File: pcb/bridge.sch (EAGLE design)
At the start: 31 parts, among them IC1 ARDUINO_PRO_MICRO, IC2 LM358D, X1 SZARKBUS, X2 RSENSE, X3 +12V

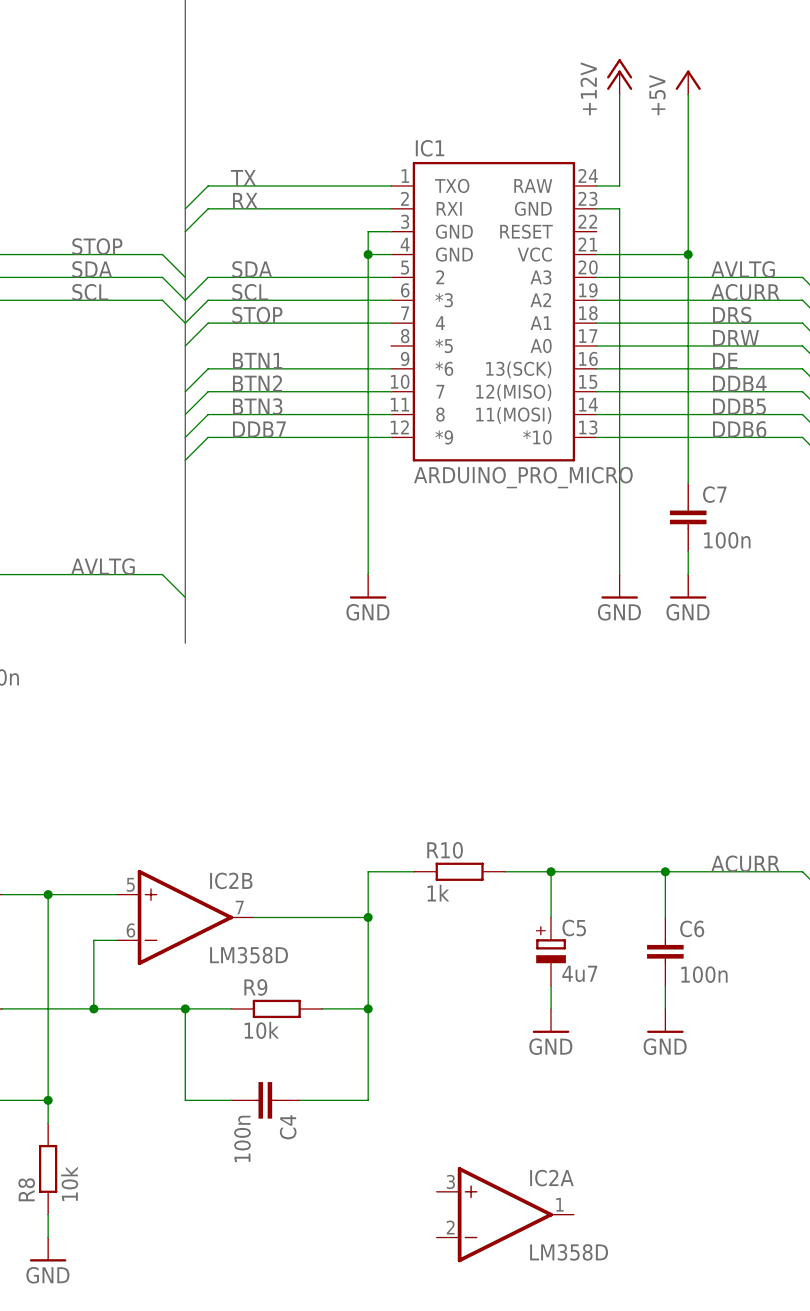
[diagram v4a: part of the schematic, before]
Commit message: bridge: Connect unused op-amp to the ground.
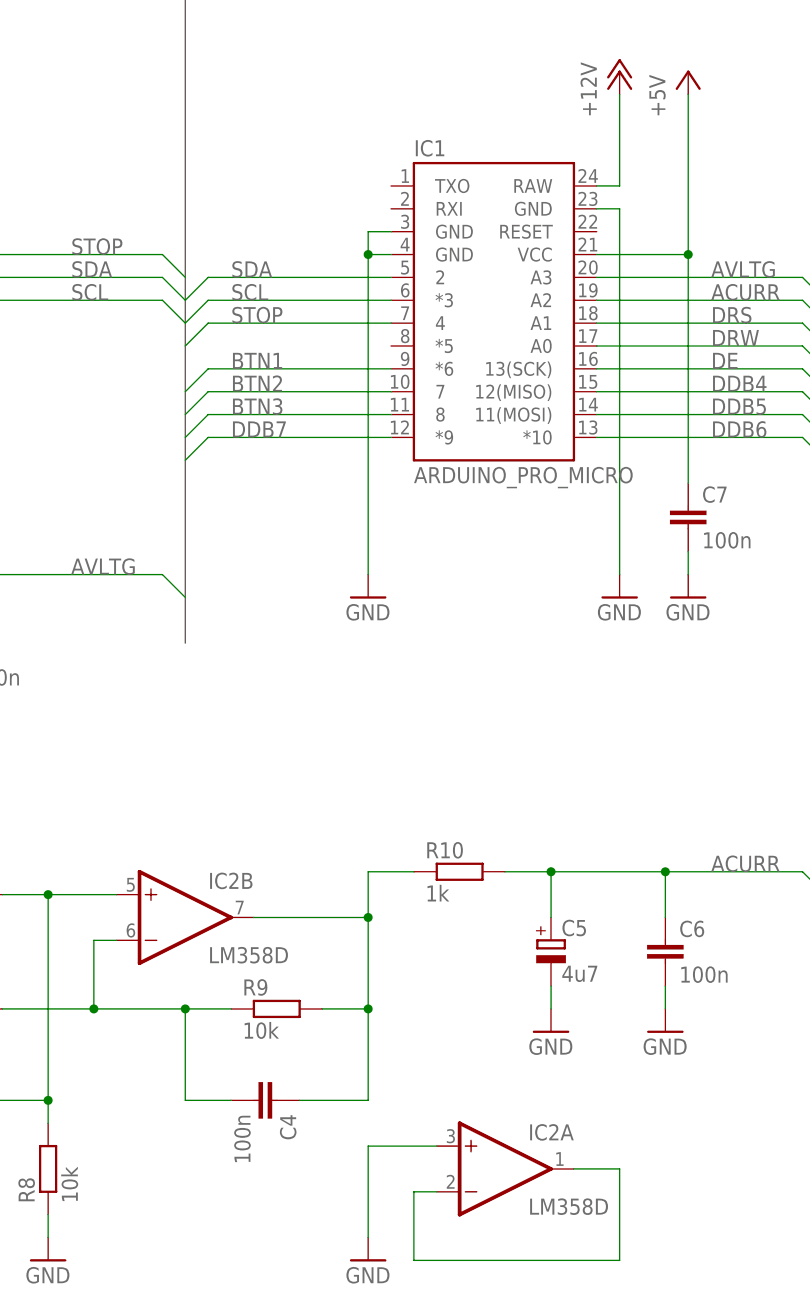
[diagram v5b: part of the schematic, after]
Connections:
- removed net RX: IC1.RXI
- removed net TX: IC1.TXO
- new net N$12: IC2A.-IN, IC2A.OUT
- net GND: now also IC2A.+IN
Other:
- moved on the sheet: IC2A
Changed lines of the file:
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@@
 <part name="C7" library="rcl" deviceset="C-EU" device="C1206" value="100n"/>
 <part name="GND15" library="supply1" deviceset="GND" device=""/>
+<part name="GND16" library="supply1" deviceset="GND" device=""/>
 </parts>
 <sheets>
@@
 <instance part="GND20" gate="1" x="215.9" y="35.56"/>
 <instance part="P+11" gate="1" x="215.9" y="66.04"/>
-<instance part="IC2" gate="A" x="139.7" y="20.32"/>
+<instance part="IC2" gate="A" x="139.7" y="25.4"/>
 <instance part="IC2" gate="B" x="104.14" y="53.34"/>
 <instance part="R6" gate="G$1" x="78.74" y="55.88"/>
@@
 <instance part="C7" gate="G$1" x="160.02" y="99.06"/>
 <instance part="GND15" gate="1" x="160.02" y="88.9"/>
+<instance part="GND16" gate="1" x="124.46" y="15.24"/>
 </instances>
 <busses>
@@
 <pinref part="GND15" gate="1" pin="GND"/>
 <wire x1="160.02" y1="91.44" x2="160.02" y2="93.98" width="0.1524" layer="91"/>
+</segment>
+<segment>
+<pinref part="IC2" gate="A" pin="+IN"/>
+<pinref part="GND16" gate="1" pin="GND"/>
+<wire x1="132.08" y1="27.94" x2="124.46" y2="27.94" width="0.1524" layer="91"/>
+<wire x1="124.46" y1="27.94" x2="124.46" y2="17.78" width="0.1524" layer="91"/>
 </segment>
 </net>
@@
 </segment>
 </net>
-<net name="RX" class="0">
-<segment>
-<wire x1="104.14" y1="129.54" x2="106.68" y2="132.08" width="0.1524" layer="91"/>
-<pinref part="IC1" gate="G$1" pin="RXI"/>
-<wire x1="106.68" y1="132.08" x2="127" y2="132.08" width="0.1524" layer="91"/>
-<label x="109.22" y="132.08" size="1.778" layer="95"/>
-</segment>
-</net>
 <net name="SDA" class="0">
 <segment>
@@
 </segment>
 </net>
-<net name="TX" class="0">
-<segment>
-<wire x1="104.14" y1="132.08" x2="106.68" y2="134.62" width="0.1524" layer="91"/>
-<pinref part="IC1" gate="G$1" pin="TXO"/>
-<wire x1="106.68" y1="134.62" x2="127" y2="134.62" width="0.1524" layer="91"/>
-<label x="109.22" y="134.62" size="1.778" layer="95"/>
-</segment>
-</net>
 <net name="BTN3" class="0">
 <segment>
@@
 </segment>
 </net>
+<net name="N$12" class="0">
+<segment>
+<pinref part="IC2" gate="A" pin="OUT"/>
+<wire x1="147.32" y1="25.4" x2="152.4" y2="25.4" width="0.1524" layer="91"/>
+<wire x1="152.4" y1="25.4" x2="152.4" y2="15.24" width="0.1524" layer="91"/>
+<wire x1="152.4" y1="15.24" x2="129.54" y2="15.24" width="0.1524" layer="91"/>
+<wire x1="129.54" y1="15.24" x2="129.54" y2="22.86" width="0.1524" layer="91"/>
+<pinref part="IC2" gate="A" pin="-IN"/>
+<wire x1="129.54" y1="22.86" x2="132.08" y2="22.86" width="0.1524" layer="91"/>
+</segment>
+</net>
 </nets>
 </sheet>
 </sheets>
+<errors>
+</errors>
 </schematic>
 </drawing>

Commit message: bridge: Update resistor values.
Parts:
- C1, C5: value 4u7 -> 22u
- R2: value 470 -> 1k
- R6, R7: value 8k2 -> 4k7
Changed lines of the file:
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@@
 <part name="P+11" library="supply1" deviceset="+12V" device=""/>
 <part name="IC2" library="linear" deviceset="LM358" device="D"/>
-<part name="R6" library="rcl" deviceset="R-EU_" device="M1206" value="8k2"/>
-<part name="R7" library="rcl" deviceset="R-EU_" device="M1206" value="8k2"/>
+<part name="R6" library="rcl" deviceset="R-EU_" device="M1206" value="4k7"/>
+<part name="R7" library="rcl" deviceset="R-EU_" device="M1206" value="4k7"/>
 <part name="R8" library="rcl" deviceset="R-EU_" device="M1206" value="10k"/>
 <part name="R9" library="rcl" deviceset="R-EU_" device="M1206" value="10k"/>
@@
 <part name="R1" library="rcl" deviceset="R-EU_" device="M1206" value="8k2"/>
 <part name="GND27" library="supply1" deviceset="GND" device=""/>
-<part name="R2" library="rcl" deviceset="R-EU_" device="M1206" value="470"/>
+<part name="R2" library="rcl" deviceset="R-EU_" device="M1206" value="1k"/>
 <part name="P+12" library="supply1" deviceset="+12V" device=""/>
 <part name="GND30" library="supply1" deviceset="GND" device=""/>
@@
 <part name="P+1" library="supply1" deviceset="+12V" device=""/>
 <part name="P+4" library="supply1" deviceset="+5V" device=""/>
-<part name="C1" library="rcl" deviceset="CPOL-EU" device="B/3528-21W" value="4u7"/>
+<part name="C1" library="rcl" deviceset="CPOL-EU" device="B/3528-21W" value="22u"/>
 <part name="GND6" library="supply1" deviceset="GND" device=""/>
-<part name="C5" library="rcl" deviceset="CPOL-EU" device="B/3528-21W" value="4u7"/>
+<part name="C5" library="rcl" deviceset="CPOL-EU" device="B/3528-21W" value="22u"/>
 <part name="GND7" library="supply1" deviceset="GND" device=""/>
 <part name="C6" library="rcl" deviceset="C-EU" device="C1206" value="100n"/>
